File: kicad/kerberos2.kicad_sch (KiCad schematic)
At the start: 64 parts, among them J1 5V, J2 3.3V, J3 1.2V, J4 GND, U1 MX25L25645G, U2 MX25L25645G, X1 SX3M12.000M20F30TNN

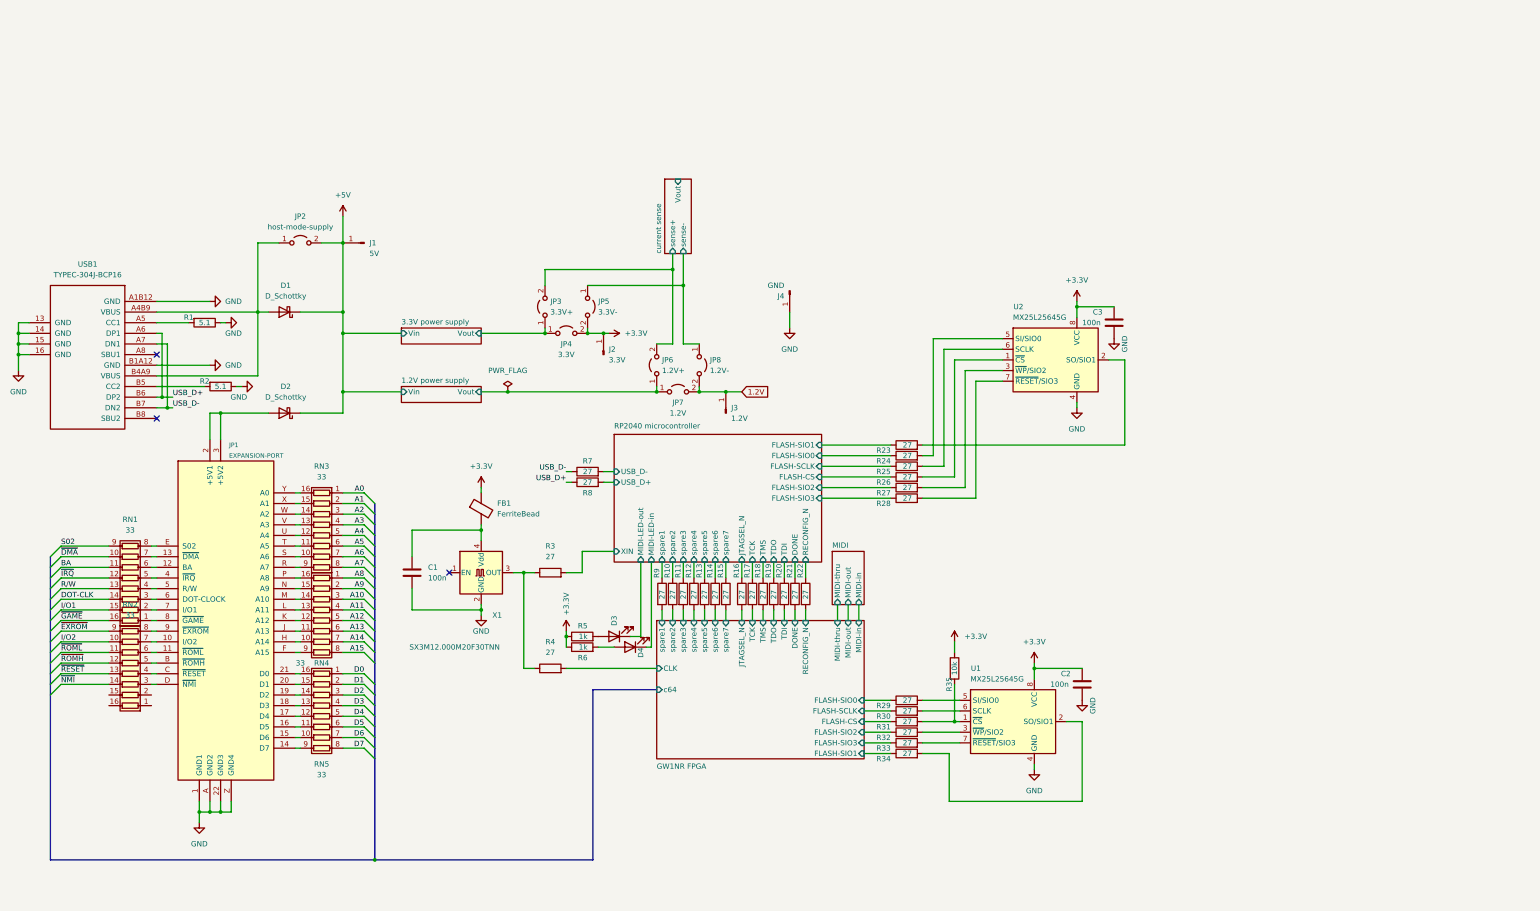
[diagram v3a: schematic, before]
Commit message: circuit improvements fixed the level shifter circuit, added the shield pins to the reset button, and replaced the IEC circuit with unused pins of the 16 bit level shifter, and a new 6 channel open collector driver
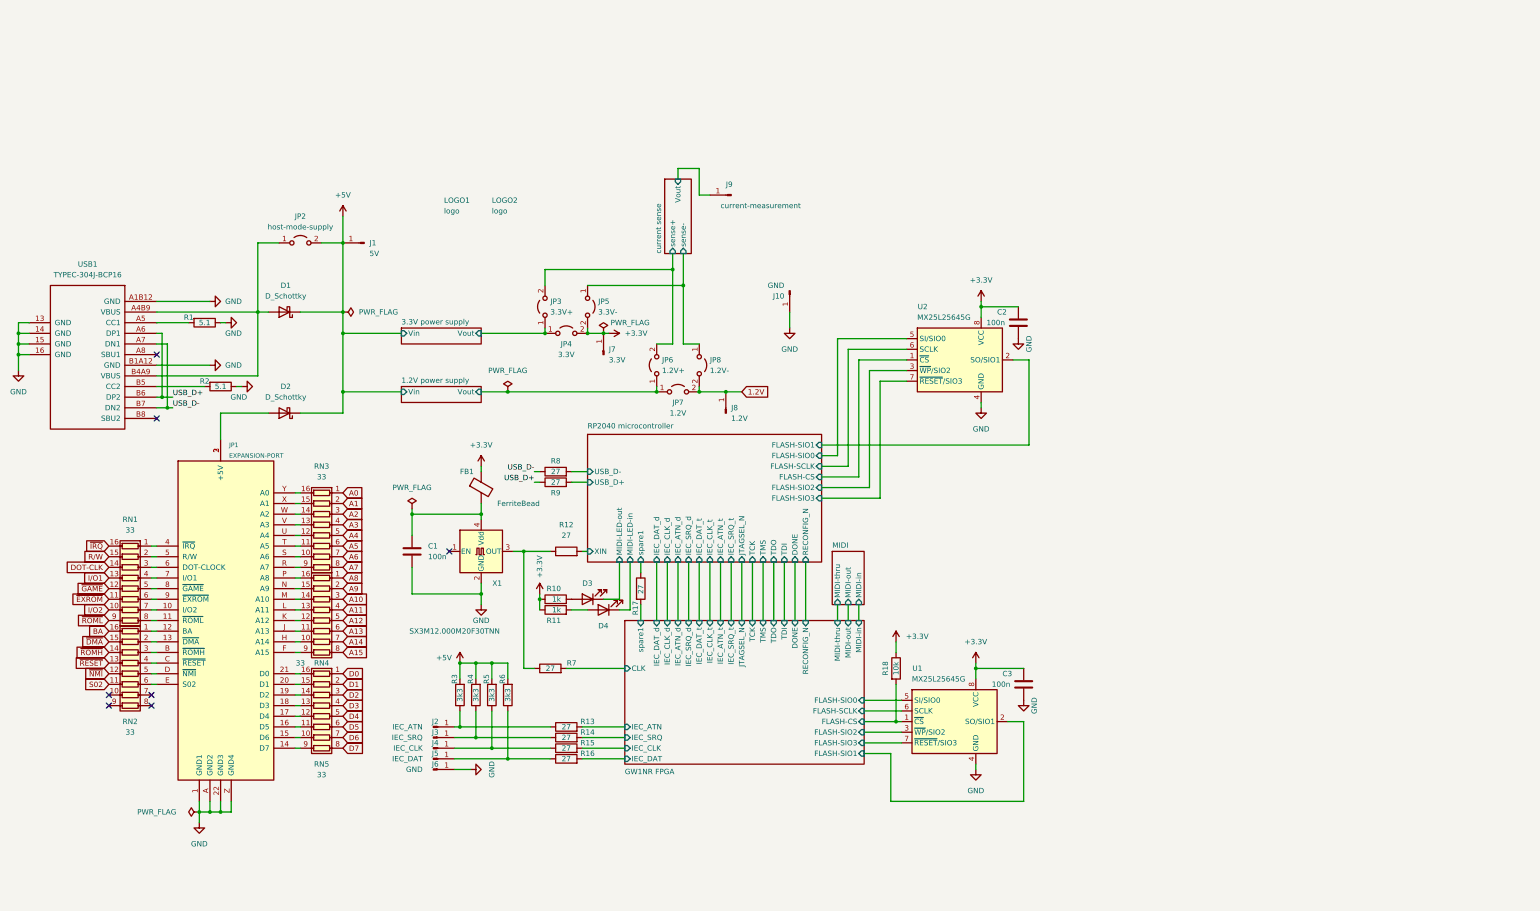
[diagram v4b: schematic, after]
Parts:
- removed R10, R11, R12, R17, R18, R19, R20, R21, R22, R23, R24, R25, R26, R27, R28, R29, R30, R31, R32, R33, R34: 27, Resistor_SMD:R_0805_2012Metric, symbol Device:R
- added J2: IEC_ATN, Connector_PinHeader_2.54mm:PinHeader_1x01_P2.54mm_Vertical, symbol Connector:Conn_01x01_Male
- added J3: IEC_SRQ, Connector_PinHeader_2.54mm:PinHeader_1x01_P2.54mm_Vertical, symbol Connector:Conn_01x01_Male
- added J4: IEC_CLK, Connector_PinHeader_2.54mm:PinHeader_1x01_P2.54mm_Vertical, symbol Connector:Conn_01x01_Male
- added J5: IEC_DAT, Connector_PinHeader_2.54mm:PinHeader_1x01_P2.54mm_Vertical, symbol Connector:Conn_01x01_Male
- added J6: GND, Connector_PinHeader_2.54mm:PinHeader_1x01_P2.54mm_Vertical, symbol Connector:Conn_01x01_Male
- added J9: current-measurement, Connector_PinHeader_2.54mm:PinHeader_1x01_P2.54mm_Vertical, symbol Connector:Conn_01x01_Male
- added LOGO1: logo, Symbol:WEEE-Logo_4.2x6mm_SilkScreen, symbol logo:logo
- added LOGO2: logo, Symbol:CE-Logo_8.5x6mm_SilkScreen, symbol logo:logo
- added R3, R4, R5, R6: 3k3, Resistor_SMD:R_0805_2012Metric, symbol Device:R
- renumbered C3 to C2, C2 to C3, J4 to J10, J2 to J7, J3 to J8, R5 to R10, R6 to R11, R3 to R12, R9 to R17, R35 to R18, R4 to R7, R7 to R8, R8 to R9
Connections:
- net +5V: now also R3.2, R4.2, R5.2, R6.2
- net BA: now also RN2.16 (R1.2); no longer RN1.11 (R6.2)
- net GND: now also J6.1 (Pin_1)
- net GW1NR FPGA/FLASH-CS: now also R18.2, U1.1 (~{CS})
- net GW1NR FPGA/FLASH-SCLK: now also U1.6 (SCLK)
- net GW1NR FPGA/FLASH-SIO0: now also U1.5 (SI/SIO0)
- net GW1NR FPGA/FLASH-SIO1: now also U1.2 (SO/SIO1)
- net GW1NR FPGA/FLASH-SIO2: now also U1.3 (~{WP}/SIO2)
- net GW1NR FPGA/FLASH-SIO3: now also U1.7 (~{RESET}/SIO3)
- net GW1NR FPGA/JTAGSEL_N: no longer R16.2
- net I/O1: now also RN1.13 (R4.2); no longer RN1.15 (R2.2)
- net I/O2: now also RN1.10 (R7.2); no longer RN2.10 (R7.2)
- net RP2040 microcontroller/FLASH-CS: now also U2.1 (~{CS})
- net RP2040 microcontroller/FLASH-SCLK: now also U2.6 (SCLK)
- net RP2040 microcontroller/FLASH-SIO0: now also U2.5 (SI/SIO0)
- net RP2040 microcontroller/FLASH-SIO1: now also U2.2 (SO/SIO1)
- net RP2040 microcontroller/FLASH-SIO2: now also U2.3 (~{WP}/SIO2)
- net RP2040 microcontroller/FLASH-SIO3: now also U2.7 (~{RESET}/SIO3)
- net R/W: now also RN1.15 (R2.2); no longer RN1.13 (R4.2)
- net S02: now also RN2.11 (R6.2); no longer RN1.9 (R8.2)
- net current sense/Vout: now also J9.1 (Pin_1)
- net ~{DMA}: now also RN2.15 (R2.2); no longer RN1.10 (R7.2)
- net ~{EXROM}: now also RN1.11 (R6.2); no longer RN2.9 (R8.2)
- net ~{GAME}: now also RN1.12 (R5.2); no longer RN1.16 (R1.2)
- net ~{IRQ}: now also RN1.16 (R1.2); no longer RN1.12 (R5.2)
- net ~{NMI}: now also RN2.12 (R5.2); no longer RN2.14 (R3.2)
- net ~{ROMH}: now also RN2.14 (R3.2); no longer RN2.12 (R5.2)
- net ~{ROML}: now also RN1.9 (R8.2); no longer RN2.11 (R6.2)
- net at RN1.1 (R1.1): now also JP1.4 (~{IRQ}); no longer JP1.8 (~{GAME})
- net at RN1.2 (R2.1): now also JP1.5 (R/W); no longer JP1.7 (I/O1)
- net at RN1.4 (R4.1): now also JP1.7 (I/O1); no longer JP1.5 (R/W)
- net at RN1.5 (R5.1): now also JP1.8 (~{GAME}); no longer JP1.4 (~{IRQ})
- net at RN1.6 (R6.1): now also JP1.9 (~{EXROM}); no longer JP1.12 (BA)
- net at RN1.7 (R7.1): now also JP1.10 (I/O2); no longer JP1.13 (~{DMA})
- net at RN1.8 (R8.1): now also JP1.11 (~{ROML}); no longer JP1.E (S02)
- net at RN2.7 (R7.1): no longer JP1.10 (I/O2)
- net at RN2.6 (R6.1): now also JP1.E (S02); no longer JP1.11 (~{ROML})
- net at RN2.8 (R8.1): no longer JP1.9 (~{EXROM})
- net at JP1.B (~{ROMH}): now also RN2.3 (R3.1); no longer RN2.5 (R5.1)
- net at JP1.D (~{NMI}): now also RN2.5 (R5.1); no longer RN2.3 (R3.1)
- net at RN2.1 (R1.1): now also JP1.12 (BA)
- net at RN2.2 (R2.1): now also JP1.13 (~{DMA})
- net GW1NR FPGA/spare5 renamed GW1NR FPGA/IEC_ATN
- net GW1NR FPGA/spare6 renamed GW1NR FPGA/IEC_SRQ
- net GW1NR FPGA/spare7 renamed GW1NR FPGA/IEC_CLK
- net RP2040 microcontroller/JTAGSEL_N: no longer names the net of R16.1
- net RP2040 microcontroller/JTAGSEL_N: now also J5.1 (Pin_1), R6.1
- net RP2040 microcontroller/spare5: no longer names the net of R13.1
- net RP2040 microcontroller/spare5: now also J2.1 (Pin_1), R3.1
- net RP2040 microcontroller/spare6: no longer names the net of R14.1
- net RP2040 microcontroller/spare6: now also J3.1 (Pin_1), R4.1
- net RP2040 microcontroller/spare7: no longer names the net of R15.1
- net RP2040 microcontroller/spare7: now also J4.1 (Pin_1), R5.1
- new net GW1NR FPGA/IEC_DAT: R16.2
- no-connect marks 3 -> 7
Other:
- sheet GW1NR FPGA ports: added IEC_ATN, IEC_ATN_d, IEC_ATN_t, IEC_CLK, IEC_CLK_d, IEC_CLK_t, IEC_DAT, IEC_DAT_d, IEC_DAT_t, IEC_SRQ, IEC_SRQ_d, IEC_SRQ_t; removed c64, spare2, spare3, spare4, spare5, spare6, spare7
- sheet RP2040 microcontroller ports: added IEC_ATN_d, IEC_ATN_t, IEC_CLK_d, IEC_CLK_t, IEC_DAT_d, IEC_DAT_t, IEC_SRQ_d, IEC_SRQ_t; removed spare2, spare3, spare4, spare5, spare6, spare7
- moved on the sheet: C1, C2, C3, D3, D4, FB1, R10, R11, R12, R17, R18, R8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

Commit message: started routing
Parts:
- R1, R2: value 5.1 -> 5k1
